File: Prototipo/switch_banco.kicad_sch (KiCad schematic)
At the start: 7 parts

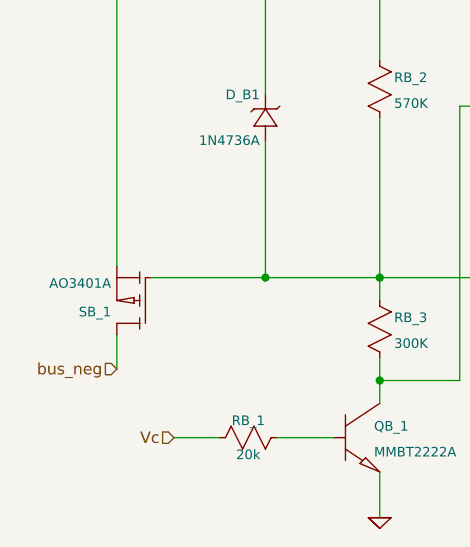
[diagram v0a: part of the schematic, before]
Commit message: Aplicar gitignore y dejar de trackear archivos innecesarios
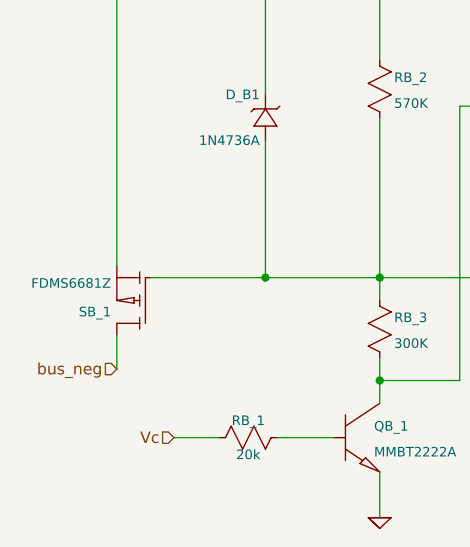
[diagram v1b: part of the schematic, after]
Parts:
- SB_1: value AO3401A -> FDMS6681Z; footprint Package_TO_SOT_SMD:SOT-23-3 -> Package_TO_SOT_SMD:PQFN_8x8
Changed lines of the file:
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@@
 			)
 		)
-		(property "Value" "AO3401A"
+		(property "Value" "FDMS6681Z"
 			(at 95.885 90.805 0)
 			(effects
@@
 			)
 		)
-		(property "Footprint" "Package_TO_SOT_SMD:SOT-23-3"
+		(property "Footprint" "Package_TO_SOT_SMD:PQFN_8x8"
 			(at 100.33 96.52 0)
 			(effects

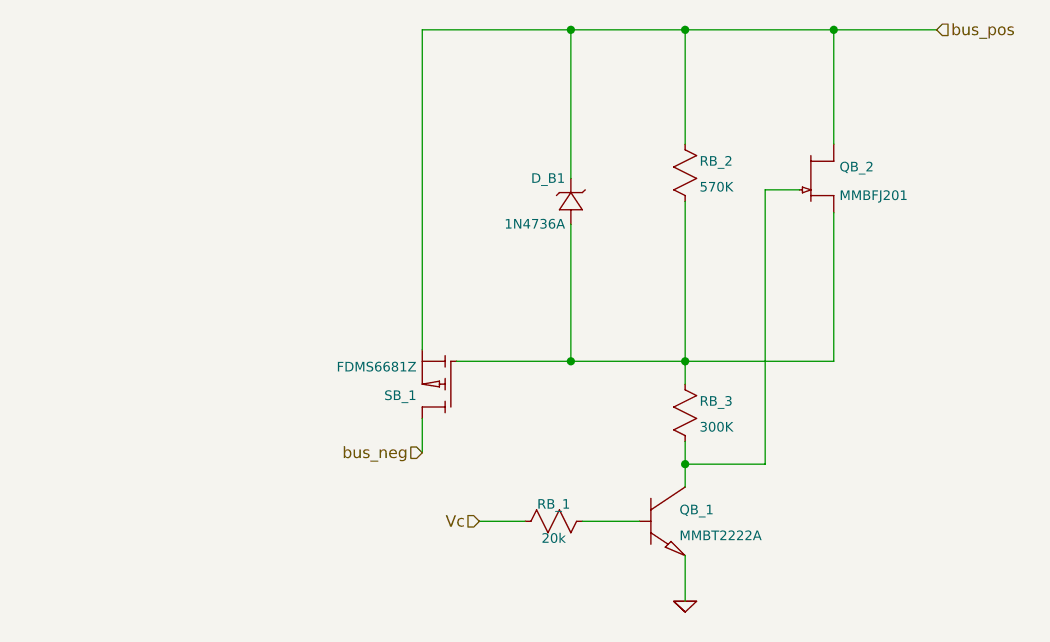
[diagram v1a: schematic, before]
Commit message: Cambios de prototipo con el nuevo pmos
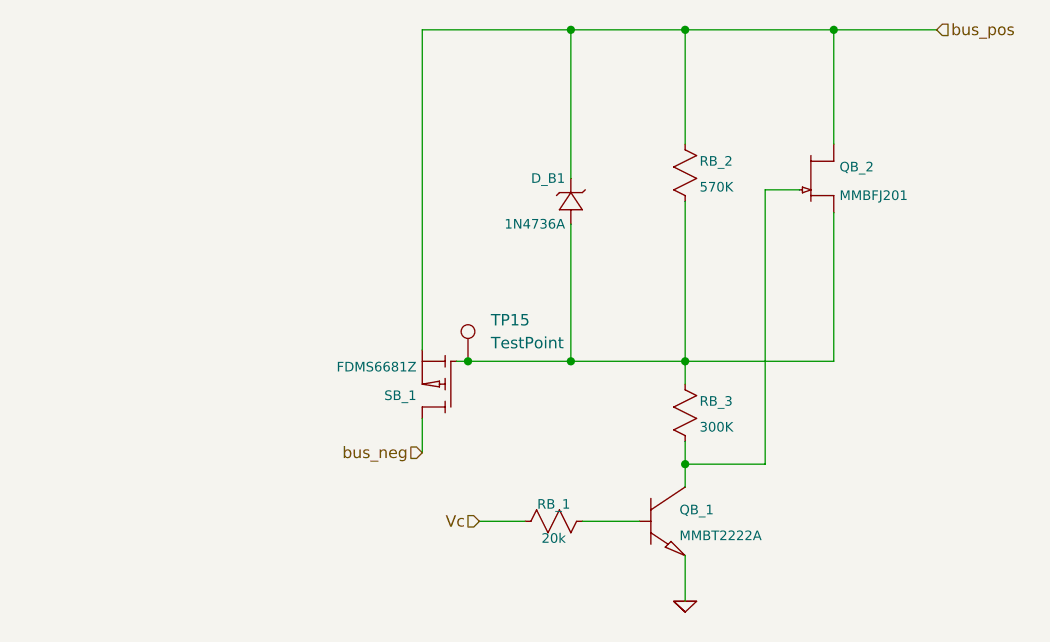
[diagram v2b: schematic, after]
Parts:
- added TP15: TestPoint, TestPoint:TestPoint_Bridge_Pitch2.54mm_Drill1.0mm, symbol Connector:TestPoint
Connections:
- net at D_B1.1 (+), QB_2.3 (S), RB_2.2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: now also TP15.1
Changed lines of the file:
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@@
+	)
+	(junction
+		(at 101.6 90.17)
+		(diameter 0)
+		(color 0 0 0 0)
 	)
 	(junction
@@
 	(wire
 		(pts
+			(xy 101.6 90.17) (xy 100.33 90.17)
+		)
+		(stroke
+			(width 0.1524)
+			(type solid)
+		)
+	)
+	(wire
+		(pts
 			(xy 142.24 66.04) (xy 142.24 53.34)
 		)
@@
 	(wire
 		(pts
-			(xy 113.03 90.17) (xy 100.33 90.17)
+			(xy 113.03 90.17) (xy 101.6 90.17)
 		)
 		(stroke
@@
 					(unit 1)
 				)
+			)
+		)
+	)
+	(symbol
+		(lib_id "Connector:TestPoint")
+		(at 101.6 90.17 0)
+		(unit 1)
+		(exclude_from_sim no)
+		(in_bom yes)
+		(on_board yes)
+		(dnp no)
+		(fields_autoplaced yes)
+		(property "Reference" "TP15"
+			(at 104.14 85.5979 0)
+			(effects
+				(font
+					(size 1.27 1.27)
+				)
+				(justify left)
+			)
+		)
+		(property "Value" "TestPoint"
+			(at 104.14 88.1379 0)
+			(effects
+				(font
+					(size 1.27 1.27)
+				)
+				(justify left)
+			)
+		)
+		(property "Footprint" "TestPoint:TestPoint_Bridge_Pitch2.54mm_Drill1.0mm"
+			(at 106.68 90.17 0)
+			(effects
+				(font
+					(size 1.27 1.27)
+				)
+				(hide yes)
+			)
+		)
+		(property "Datasheet" "~"
+			(at 106.68 90.17 0)
+			(effects
+				(font
+					(size 1.27 1.27)
+				)
+				(hide yes)
+			)
+		)
+		(property "Description" "test point"
+			(at 101.6 90.17 0)
+			(effects
+				(font
+					(size 1.27 1.27)
+				)
+				(hide yes)
+			)
+		)
+		(pin "1"
+		)
+		(instances
+			(project "prototipo"
+				(path "/c9225433-a7fd-41e8-8162-e91e829dcb79/69120eb2-13db-48bd-9e77-f62722c18bbc"
+					(reference "TP17")
+					(unit 1)
+				)
+				(path "/c9225433-a7fd-41e8-8162-e91e829dcb79/7c9a14ee-10ad-4ddf-af17-6bfeb468e011"
+					(reference "TP15")
+					(unit 1)
+				)
+				(path "/c9225433-a7fd-41e8-8162-e91e829dcb79/aa26f19e-f2c7-49c1-961b-509062eddf74"
+					(reference "TP16")
+					(unit 1)
+				)

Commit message: ruteo de dos celdas más
Chequear la orientación de los portapilas
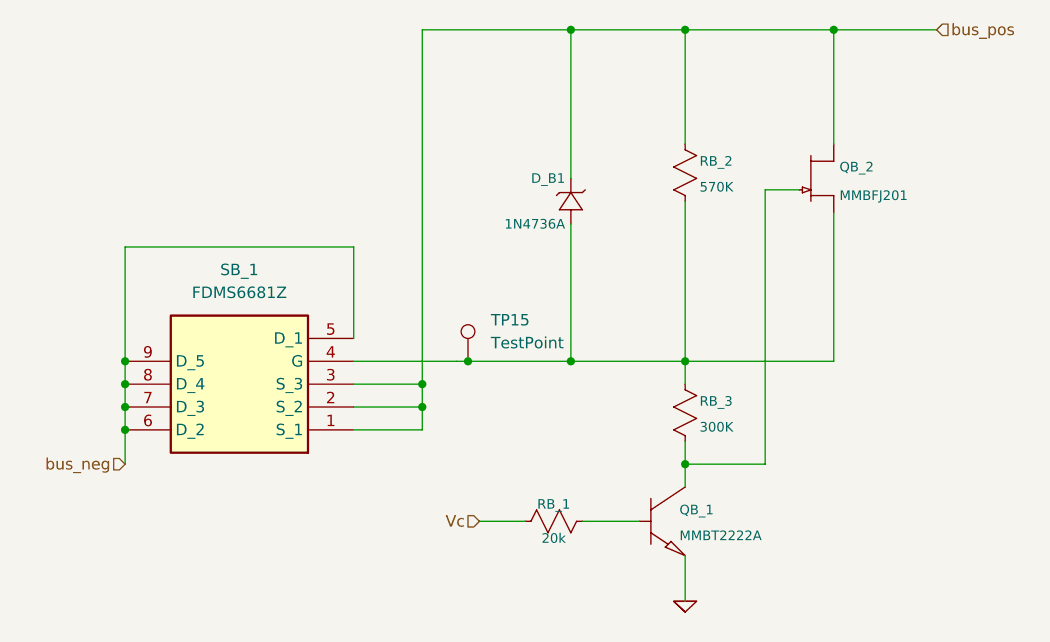
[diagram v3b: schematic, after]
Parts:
- removed SB_1: FDMS6681Z, Package_TO_SOT_SMD:PQFN_8x8, symbol ltspice:pmos
- added SB_1: FDMS6681Z, FDMS6681Z, symbol FDMS6681Z:FDMS6681Z
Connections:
- net bus_neg: now also SB_1.5 (D_1), SB_1.6 (D_2), SB_1.7 (D_3), SB_1.8 (D_4), SB_1.9 (D_5)
- net bus_pos: now also SB_1.1 (S_1), SB_1.2 (S_2), SB_1.3 (S_3)
- net at D_B1.1 (+), QB_2.3 (S), RB_2.2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: now also SB_1.4 (G)
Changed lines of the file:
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@@
+	)
+	(junction
+		(at 63.5 97.79)
+		(diameter 0)
+		(color 0 0 0 0)
+	)
+	(junction
+		(at 96.52 95.25)
+		(diameter 0)
+		(color 0 0 0 0)
 	)
 	(junction
@@
 	)
 	(junction
+		(at 63.5 95.25)
+		(diameter 0)
+		(color 0 0 0 0)
+	)
+	(junction
+		(at 63.5 92.71)
+		(diameter 0)
+		(color 0 0 0 0)
+	)
+	(junction
 		(at 125.73 90.17)
+		(diameter 0)
+		(color 0 0 0 0)
+	)
+	(junction
+		(at 63.5 90.17)
+		(diameter 0)
+		(color 0 0 0 0)
+	)
+	(junction
+		(at 96.52 92.71)
 		(diameter 0)
 		(color 0 0 0 0)
@@
 	(wire
 		(pts
-			(xy 96.52 100.33) (xy 96.52 96.52)
+			(xy 63.5 101.6) (xy 63.5 97.79)
 		)
 		(stroke
@@
 	(wire
 		(pts
+			(xy 96.52 95.25) (xy 96.52 97.79)
+		)
+		(stroke
+			(width 0)
+			(type default)
+		)
+	)
+	(wire
+		(pts
+			(xy 88.9 77.47) (xy 63.5 77.47)
+		)
+		(stroke
+			(width 0)
+			(type default)
+		)
+	)
+	(wire
+		(pts
+			(xy 63.5 77.47) (xy 63.5 90.17)
+		)
+		(stroke
+			(width 0)
+			(type default)
+		)
+	)
+	(wire
+		(pts
+			(xy 96.52 92.71) (xy 96.52 95.25)
+		)
+		(stroke
+			(width 0)
+			(type default)
+		)
+	)
+	(wire
+		(pts
 			(xy 113.03 90.17) (xy 113.03 74.93)
 		)
@@
 	(wire
 		(pts
+			(xy 96.52 97.79) (xy 88.9 97.79)
+		)
+		(stroke
+			(width 0)
+			(type default)
+		)
+	)
+	(wire
+		(pts
 			(xy 113.03 69.85) (xy 113.03 53.34)
 		)
@@
 	(wire
 		(pts
-			(xy 96.52 88.9) (xy 96.52 53.34)
-		)
-		(stroke
-			(width 0.1524)
-			(type solid)
+			(xy 96.52 53.34) (xy 96.52 92.71)
+		)
+		(stroke
+			(width 0)
+			(type default)
+		)
+	)
+	(wire
+		(pts
+			(xy 96.52 92.71) (xy 88.9 92.71)
+		)
+		(stroke
+			(width 0)
+			(type default)
+		)
+	)
+	(wire
+		(pts
+			(xy 88.9 90.17) (xy 100.33 90.17)
+		)
+		(stroke
+			(width 0)
+			(type default)
+		)
+	)
+	(wire
+		(pts
+			(xy 63.5 90.17) (xy 63.5 92.71)
+		)
+		(stroke
+			(width 0)
+			(type default)
+		)
+	)
+	(wire
+		(pts
+			(xy 63.5 92.71) (xy 63.5 95.25)
+		)
+		(stroke
+			(width 0)
+			(type default)
 		)
 	)
@@
 	(wire
 		(pts
+			(xy 88.9 87.63) (xy 88.9 77.47)
+		)
+		(stroke
+			(width 0)
+			(type default)
+		)
+	)
+	(wire
+		(pts
 			(xy 125.73 101.6) (xy 125.73 99.06)
 		)
@@
 			(width 0.1524)
 			(type solid)
+		)
+	)
+	(wire
+		(pts
+			(xy 96.52 95.25) (xy 88.9 95.25)
+		)
+		(stroke
+			(width 0)
+			(type default)
+		)
+	)
+	(wire
+		(pts
+			(xy 63.5 95.25) (xy 63.5 97.79)
+		)
+		(stroke
+			(width 0)
+			(type default)
 		)
 	)
@@
 	(hierarchical_label "bus_neg"
 		(shape input)
-		(at 96.52 100.33 180)
+		(at 63.5 101.6 180)
 		(effects
 			(font
@@
 			)
 			(justify right)
-		)
-	)
-	(symbol
-		(lib_name "pmos_1")
-		(lib_id "ltspice:pmos")
-		(at 100.33 96.52 180)
-		(unit 1)
-		(exclude_from_sim no)
-		(in_bom yes)
-		(on_board yes)
-		(dnp no)
-		(property "Reference" "SB_1"
-			(at 95.885 93.98 0)
-			(effects
-				(font
-					(size 1.0668 1.0668)
-				)
-				(justify left)
-			)
-		)
-		(property "Value" "FDMS6681Z"
-			(at 95.885 90.805 0)
-			(effects
-				(font
-					(size 1.0668 1.0668)
-				)
-				(justify left)
-			)
-		)
-		(property "Footprint" "Package_TO_SOT_SMD:PQFN_8x8"
-			(at 100.33 96.52 0)
-			(effects
-				(font
-					(size 1.27 1.27)
-				)
-				(hide yes)
-			)
-		)
-		(property "Datasheet" ""
-			(at 100.33 96.52 0)
-			(effects
-				(font
-					(size 1.27 1.27)
-				)
-				(hide yes)
-			)
-		)
-		(property "Description" ""
-			(at 100.33 96.52 0)
-			(effects
-				(font
-					(size 1.27 1.27)
-				)
-				(hide yes)
-			)
-		)
-		(property "Sim.Library" "C:\\Users\\---\\AppData\\Local\\LTspice\\lib\\sub\\AO3401A.sub"
-			(at 100.33 96.52 0)
-			(effects
-				(font
-					(size 1.27 1.27)
-				)
-				(hide yes)
-			)
-		)
-		(property "Sim.Device" "SUBCKT"
-			(at 100.33 96.52 0)
-			(effects
-				(font
-					(size 1.27 1.27)
-				)
-				(hide yes)
-			)
-		)
-		(property "Sim.Params" "model=\"AO3401A\""
-			(at 100.33 96.52 0)
-			(effects
-				(font
-					(size 1.27 1.27)
-				)
-				(hide yes)
-			)
-		)
-		(pin "3"
-		)
-		(pin "2"
-		)
-		(pin "1"
-		)
-		(instances
-			(project "prototipo"
-				(path "/c9225433-a7fd-41e8-8162-e91e829dcb79/69120eb2-13db-48bd-9e77-f62722c18bbc"
-					(reference "SB_3")
-					(unit 1)
-				)
-				(path "/c9225433-a7fd-41e8-8162-e91e829dcb79/7c9a14ee-10ad-4ddf-af17-6bfeb468e011"
-					(reference "SB_1")
-					(unit 1)
-				)
-				(path "/c9225433-a7fd-41e8-8162-e91e829dcb79/aa26f19e-f2c7-49c1-961b-509062eddf74"
-					(reference "SB_2")
-					(unit 1)
-				)
-			)
 		)
 	)
@@
 					(unit 1)
 				)
+			)
+		)
+	)
+	(symbol
+		(lib_id "FDMS6681Z:FDMS6681Z")
+		(at 88.9 97.79 180)
+		(unit 1)
+		(exclude_from_sim no)
+		(in_bom yes)
+		(on_board yes)
+		(dnp no)
+		(fields_autoplaced yes)
+		(property "Reference" "SB_1"
+			(at 76.2 80.01 0)
+			(effects
+				(font
+					(size 1.27 1.27)
+				)
+			)
+		)
+		(property "Value" "FDMS6681Z"
+			(at 76.2 82.55 0)
+			(effects
+				(font
+					(size 1.27 1.27)
+				)
+			)
+		)
+		(property "Footprint" "FDMS6681Z"
+			(at 67.31 2.87 0)
+			(effects
+				(font
+					(size 1.27 1.27)
+				)
+				(justify left top)
+				(hide yes)
+			)
+		)
+		(property "Datasheet" "https://www.onsemi.com/pub/Collateral/FDMS6681Z-D.PDF"
+			(at 67.31 -97.13 0)
+			(effects
+				(font
+					(size 1.27 1.27)
+				)
+				(justify left top)
+				(hide yes)
+			)
+		)
+		(property "Description" "Max rDS(on) = 5.0 m at VGS = -4.5 V, ID = -15.7 A ; HBM ESD protection level of 8kV typical (Note 3); RoHS Compliant ; Advanced Package and Silicon combination for low rDS(on) and high efficiency ; Max rDS(on) = 3.2 m at VGS = -10 V, ID = -21.1 A ; MSL1 robust package design"
+			(at 88.9 97.79 0)
+			(effects
+				(font
+					(size 1.27 1.27)
+				)
+				(hide yes)
+			)
+		)
+		(property "Height" "1.1"
+			(at 67.31 -297.13 0)
+			(effects
+				(font
+					(size 1.27 1.27)
+				)
+				(justify left top)
+				(hide yes)
+			)
+		)
+		(property "Mouser Part Number" "512-FDMS6681Z"
+			(at 67.31 -397.13 0)
+			(effects
+				(font
+					(size 1.27 1.27)
+				)
+				(justify left top)
+				(hide yes)
+			)
+		)
+		(property "Mouser Price/Stock" "https://www.mouser.co.uk/ProductDetail/ON-Semiconductor-Fairchild/FDMS6681Z?qs=eQsPqqG3NqYIemB4oC6BVw%3D%3D"
+			(at 67.31 -497.13 0)
+			(effects
+				(font
+					(size 1.27 1.27)
+				)
+				(justify left top)
+				(hide yes)
+			)
+		)
+		(property "Manufacturer_Name" "onsemi"
+			(at 67.31 -597.13 0)
+			(effects
+				(font
+					(size 1.27 1.27)
+				)
+				(justify left top)
+				(hide yes)
+			)
+		)
+		(property "Manufacturer_Part_Number" "FDMS6681Z"
+			(at 67.31 -697.13 0)
+			(effects
+				(font
+					(size 1.27 1.27)
+				)
+				(justify left top)
+				(hide yes)
+			)
+		)
+		(pin "5"
+		)
+		(pin "6"
+		)
+		(pin "1"
+		)
+		(pin "3"
+		)
+		(pin "8"
+		)
+		(pin "2"
+		)
+		(pin "4"
+		)
+		(pin "7"
+		)
+		(pin "9"
+		)
+		(instances
+			(project ""
+				(path "/c9225433-a7fd-41e8-8162-e91e829dcb79/69120eb2-13db-48bd-9e77-f62722c18bbc"
+					(reference "Q21")
+					(unit 1)
+				)
+				(path "/c9225433-a7fd-41e8-8162-e91e829dcb79/7c9a14ee-10ad-4ddf-af17-6bfeb468e011"
+					(reference "SB_1")
+					(unit 1)
+				)
+				(path "/c9225433-a7fd-41e8-8162-e91e829dcb79/aa26f19e-f2c7-49c1-961b-509062eddf74"
+					(reference "Q20")
+					(unit 1)
+				)

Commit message: Agrega los fusibles en los bancos
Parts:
- added F7: Fuse, Huellas:Fuseholder_Cylinder-5x20mm_Schurter_0031_8201_Horizontal_Open, symbol Device:Fuse
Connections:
- net bus_neg: now also F7.2; no longer SB_1.5 (D_1), SB_1.6 (D_2), SB_1.7 (D_3), SB_1.8 (D_4), SB_1.9 (D_5)
- new net: F7.1, SB_1.5 (D_1), SB_1.6 (D_2), SB_1.7 (D_3), SB_1.8 (D_4), SB_1.9 (D_5)
